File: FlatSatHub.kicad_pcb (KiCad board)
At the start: 4 copper layers, 166.3 x 166.3 mm, 218 parts, among them J1 Jack-DC, J10 DB26_Male_HighDensity_Mountin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, J12 DB26_Male_HighDensity_Mountin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, J14 DB26_Male_HighDensity_Mountin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, J16 DB26_Male_HighDensity_Mountin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, J17 Conn_01x06, J2 Conn_01x06, J3 Conn_01x06, J4 DB26_Male_HighDensity_Mountin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, J5 DB26_Male_HighDensity_Mountin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, J6 DB26_Male_HighDensity_Mountin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, J8 DB26_Male_HighDensity_Mountin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, SW1 SW_DIP_x03, SW10 SW_DIP_x02, SW11 SW_Push, SW2 SW_DIP_x03, SW3 SW_DIP_x03, SW4 SW_DIP_x03, SW5 SW_DIP_x03, SW6 SW_DIP_x03, SW7 SW_DIP_x03, SW8 SW_DIP_x03, U1 TPS54560B, U10 TPS22917DBV, U11 BTS6163D, U12 TPS22917DBV, U13 TPS22917DBV, U14 BTS6163D, U15 TPS22917DBV, U16 TPS22917DBV, U17 BTS6163D, U18 TPS22917DBV, U19 TPS22917DBV, U2 TPS54560B, U20 BTS6163D, U21 TPS22917DBV, U22 TPS22917DBV, U23 BTS6163D, U24 TPS22917DBV, U25 TPS22917DBV, U26 BTS6163D, U27 TPS22917DBV, U28 TPS22917DBV, U29 BTS6163D, U3 ASDMB-xxxMHz, U30 TPS22917DBV, U31 TPS22917DBV, U32 BTS6163D, U4 ICE40HX1K-4K-TQ144, U5 M25PX32-VMW, U6 tps6240x, U7 TLV73325PDBV, U8 TPS54560B, U9 TPS22917DBV

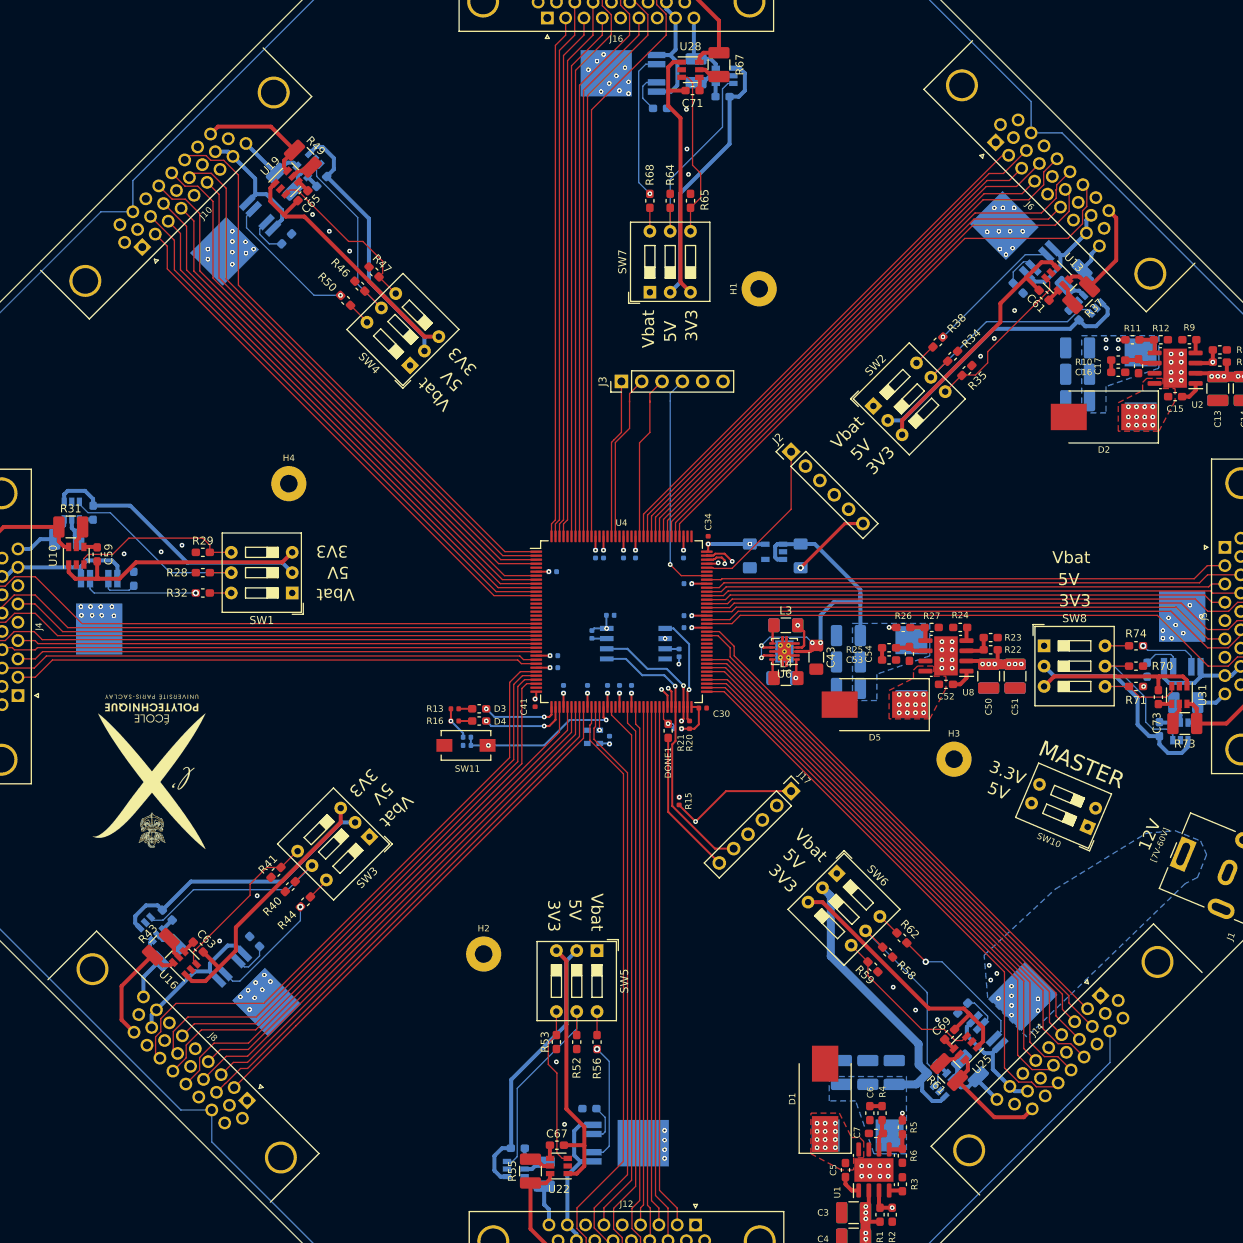
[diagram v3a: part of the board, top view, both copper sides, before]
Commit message: Last few silk screen cleanups
Signed-off-by: Alexis Jeandet <alexis.jeandet@member.fsf.org>
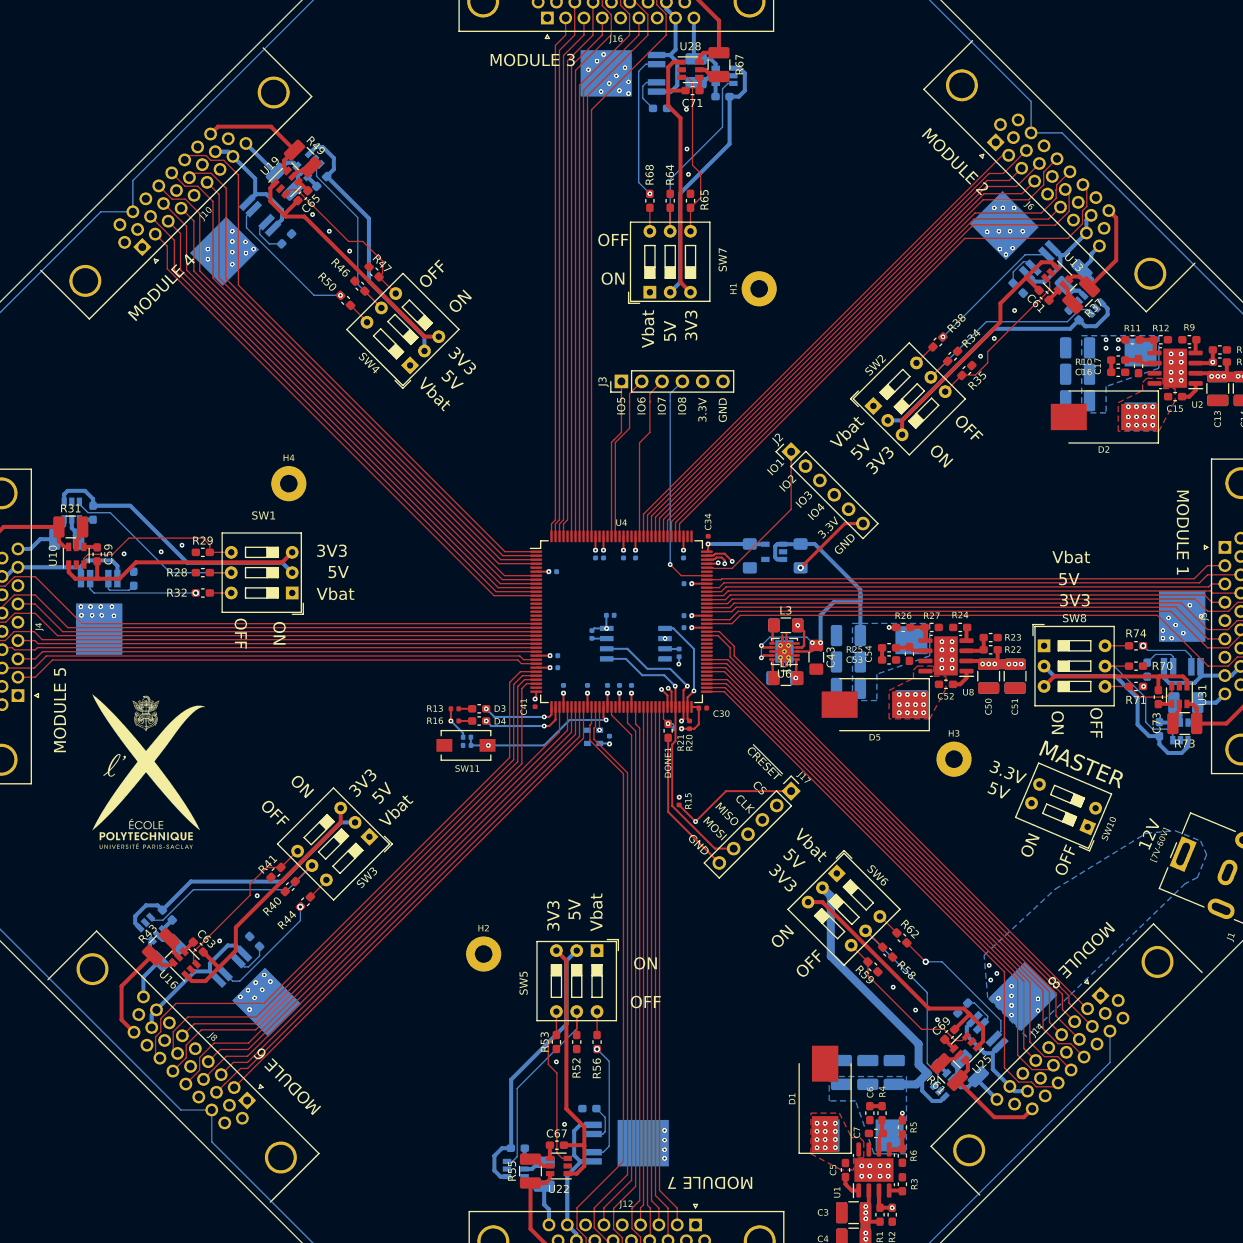
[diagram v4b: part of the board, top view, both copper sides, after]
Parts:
- turned LOGO1 to 0 degrees
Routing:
- net VCCIO_0: track 61.9 -> 73.4 mm
- net GND: track 33.6 -> 36.6 mm
- net /Sheet5F604EE5/FLASH_CLK: track 36.2 -> 36.8 mm
- net /FPGA_2.5V: vias 2 -> 1
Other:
- board text added: "CLK"
- board text added: "CS"
- board text added: "GND"
- board text added: "IO1"
- board text added: "IO2"
- board text added: "IO3"
- board text added: "IO4"
- board text added: "IO5"
- board text added: "IO6"
- board text added: "IO7"
- board text added: "IO8"
- board text added: "MISO"
- board text added: "MODULE 1"
- board text added: "MODULE 2"
- board text added: "MODULE 3"
- board text added: "MODULE 4"
- board text added: "MODULE 5"
- board text added: "MODULE 6"
- board text added: "MODULE 7"
- board text added: "MODULE 8"
- board text added: "MOSI"
- board text added: "OFF ON"
- board text added: "ON OFF"
- board text added: "~CRESET"
